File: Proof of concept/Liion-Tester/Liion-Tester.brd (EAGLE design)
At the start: 100 x 80 mm, 22 parts, among them Q1 BC327, Q2 SI4403DDY-T1-GE3, U1 1042, U2 NCP1854FCCT1G, U3 BQ27427YZFR

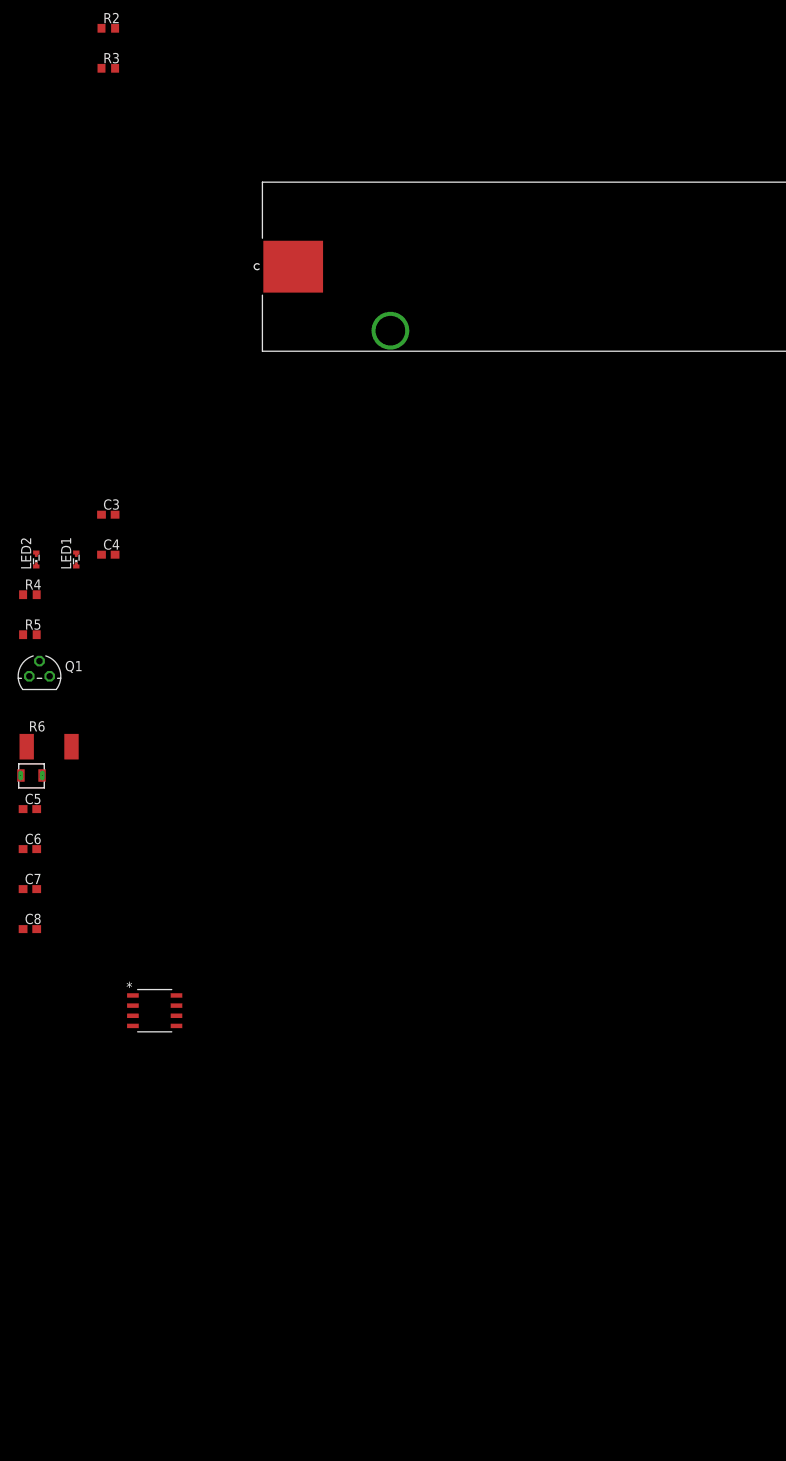
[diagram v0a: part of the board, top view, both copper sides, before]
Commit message: Rework of BQ and NCP. Connector added to schematic.
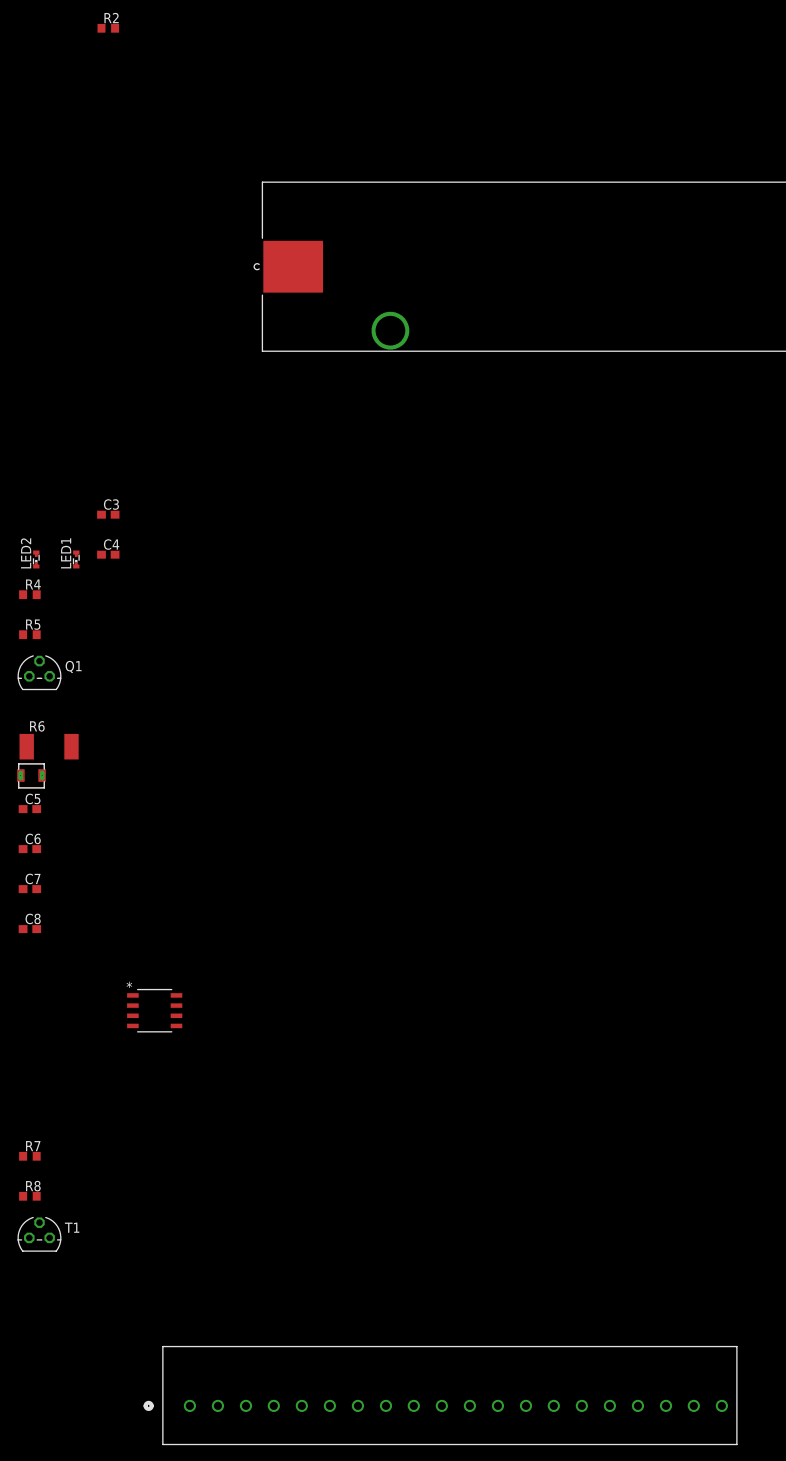
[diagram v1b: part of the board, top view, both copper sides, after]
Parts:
- removed R3: 1M8, rcl:R0603
- added J1: 250-120, custom_library:CONN_250-120_WAG
- added R7, R8: 3k3, rcl:R0603
- added T1: BC337, transistor:TO92
- L1: value 2u2 -> 2.2uH
- renumbered U$1 to L1
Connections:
- removed net GPOUT: R2.1, U3.A1
- removed net VSYS: U3.C2
- new net GPOUT_BQ: J1.5, R2.1, U3.A1
- new net N$9: LED1.A@1, T1.1
- net +5V: now also J1.1, R4.2, R7.2, R8.2; no longer R3.2
- net FTRY: now also J1.9
- net GND: now also J1.2
- net ILIM1: now also J1.10
- net ILIM2: now also J1.11
- net LED_IND: now also J1.6, T1.2; no longer R4.2
- net N$2: no longer R3.1
- net N$4: now also T1.3; no longer LED1.A@1
- net OTG: now also J1.12
- net PACK_P: now also U3.C2
- net SCL: now also J1.3, R7.1
- net SDA: now also J1.4, R8.1
- net SENSN: now also J1.8
- net SPM: now also J1.7
- net TRANS: now also J1.13

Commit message: Final changes in .sch before making .brd
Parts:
- removed J1: 250-120, custom_library:CONN_250-120_WAG
- removed LED1: RED, led:SMARTLED-TTW
- removed Q1: BC327, transistor-pnp:TO92
- removed R4: 3k3, rcl:R0603
- removed T1: BC337, transistor:TO92
- added JUMPERS: (no value), pinhead:2X02
- added MCU: 250-109, custom_library:CONN_250-109_WAG
- added POWER, USB: 250-102, custom_library:CONN_250-102_WAG
- R7, R8: value 3k3 -> 3k3-DNP
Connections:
- removed net N$4: R4.1, T1.3
- removed net N$6: Q1.3, R5.1
- removed net N$9: LED1.A@1, T1.1
- new net BAT_NCP: JUMPERS.3, U2.E5
- new net SRX_BQ: JUMPERS.1, U3.C2
- net +5V: now also POWER.1; no longer J1.1, R4.2, R5.2
- net FTRY: now also MCU.7; no longer J1.9
- net GND: now also POWER.2; no longer J1.2, LED1.C@1
- net GPOUT_BQ: now also MCU.3; no longer J1.5
- net ILIM1: now also MCU.8; no longer J1.10
- net ILIM2: now also MCU.9; no longer J1.11
- net LED_IND: now also MCU.4, R5.2; no longer J1.6, Q1.2, T1.2
- net N$5: now also R5.1; no longer Q1.1
- net OTG: now also USB.1; no longer J1.12
- net PACK_P: now also JUMPERS.2, JUMPERS.4; no longer U2.E5, U3.C2
- net SCL: now also MCU.1; no longer J1.3
- net SDA: now also MCU.2; no longer J1.4
- net SENSN: now also MCU.6; no longer J1.8
- net SPM: now also MCU.5; no longer J1.7
- net TRANS: now also USB.2; no longer J1.13

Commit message: Version control
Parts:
- R7, R8: value 3k3-DNP -> DNP-3k3
- moved JUMPERS 370.6 mm to (34.4, 51.4), turned to 180 degrees
- moved MCU 353.4 mm to (62.6, 49.8)
- moved USB 311.3 mm to (53.4, 49.8)
- moved POWER 296.6 mm to (44.2, 49.8)
- moved R8 277.6 mm to (66.0, 54.0), flipped to the bottom, turned to 90 degrees
- moved R7 271.8 mm to (62.6, 54.0), flipped to the bottom, turned to 90 degrees
- moved C8 262.3 mm to (62.0, 72.6), flipped to the bottom, turned to 180 degrees
- moved Q2 262.2 mm to (70.2, 64.6), flipped to the bottom, turned to 180 degrees
- moved C7 256.0 mm to (57.2, 72.6), flipped to the bottom, turned to 180 degrees
- moved C6 251.6 mm to (66.8, 69.6), flipped to the bottom, turned to 180 degrees
- moved C5 245.3 mm to (53.2, 72.6), flipped to the bottom, turned to 180 degrees
- moved L1 237.7 mm to (54.0, 68.6), flipped to the bottom, turned to 270 degrees
- moved R6 236.3 mm to (60.6, 69.2), flipped to the bottom
- moved R5 217.2 mm to (60.4, 62.0), flipped to the bottom, turned to 90 degrees
- moved C4 205.5 mm to (53.8, 65.6), flipped to the bottom
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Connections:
- net BAT_NCP: now also JUMPERS.1; no longer JUMPERS.3
- net SRX_BQ: now also JUMPERS.3; no longer JUMPERS.1
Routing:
- net PACK_P: track 0.00 -> 103.2 mm, vias 0 -> 3
- net +5V: track 0.00 -> 58.2 mm, vias 0 -> 2
- net SDA: track 0.00 -> 43.5 mm, vias 0 -> 3
- net SENSN: track 0.00 -> 40.2 mm, vias 0 -> 1
- net SCL: track 0.00 -> 37.5 mm, vias 0 -> 2
- net BAT_NCP: track 0.00 -> 34.9 mm, vias 0 -> 1
- net SPM: track 0.00 -> 34.4 mm
- net FTRY: track 0.00 -> 31.5 mm
- net N$5: track 0.00 -> 27.4 mm, vias 0 -> 3
- net SRX_BQ: track 0.00 -> 21.8 mm, vias 0 -> 1
- net LED_IND: track 0.00 -> 21.7 mm
- net N$7: track 0.00 -> 11.8 mm
- net FET: track 0.00 -> 9.98 mm
- net CBOOT: track 0.00 -> 9.08 mm, vias 0 -> 2
- net TRANS: track 0.00 -> 8.96 mm, vias 0 -> 1
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- added copper zone on layer 1, net GND
- added copper zone on layer 16, net GND

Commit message: Finished .brd with changes in schematic
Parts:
- removed LED2: GREEN, led:SMARTLED-TTW
- added LED1: FYLS-1206PGC, custom_library:LED_QBLP650_1206_QTB
- moved R7 10.0 mm to (69.6, 46.8), turned to 270 degrees
- moved R8 7.20 mm to (66.2, 46.8), turned to 270 degrees
- moved L1 5.43 mm to (48.6, 69.2), turned to 90 degrees
- moved C8 5.00 mm to (57.0, 72.6)
- moved C7 3.60 mm to (60.8, 72.6)
- moved R6 2.81 mm to (57.8, 69.0)
- moved JUMPERS 1.22 mm to (33.2, 51.2)
- moved U2 0.85 mm to (58.0, 65.2)
- moved R1 0.45 mm to (37.0, 68.0)
- moved U3 0.28 mm to (40.7, 68.1)
- moved C4 0.28 mm to (53.6, 65.8)
- moved C3 0.20 mm to (53.6, 63.4)
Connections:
- removed net N$5: LED2.A@1, R5.1
- new net N$4: LED1.2, R5.1
- net FTRY: now also MCU.6; no longer MCU.7
- net GND: now also LED1.1; no longer LED2.C@1
- net GPOUT_BQ: now also MCU.5; no longer MCU.3
- net ILIM2: now also MCU.7; no longer MCU.9
- net OTG: now also USB.2; no longer USB.1
- net SCL: now also MCU.3; no longer MCU.1
- net SENSN: now also MCU.9; no longer MCU.6
- net SPM: now also MCU.1; no longer MCU.5
- net TRANS: now also USB.1; no longer USB.2
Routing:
- net GPOUT_BQ: track 2.68 -> 57.4 mm, vias 0 -> 3
- net ILIM1: track 0.00 -> 35.1 mm
- net ILIM2: track 0.00 -> 31.6 mm
- net N$5: track 27.4 -> 0.00 mm, vias 3 -> 0
- net N$4: track 0.00 -> 24.8 mm, vias 0 -> 1
- net OTG: track 0.00 -> 16.6 mm, vias 0 -> 3
- net TRANS: track 8.96 -> 25.1 mm, vias 1 -> 3
- net SPM: track 34.4 -> 18.4 mm, vias 0 -> 2
- net SENSN: track 40.2 -> 55.6 mm, vias 1 -> 0
- net SENSP: track 4.11 -> 12.0 mm, vias 0 -> 2
- net N$8: track 0.00 -> 7.41 mm
- net SCL: track 37.5 -> 42.7 mm, vias 2 -> 3
- net BAT_NCP: track 34.9 -> 39.2 mm, vias 1 -> 4
- net +5V: track 58.2 -> 62.3 mm, vias 2 -> 1
- net N$7: track 11.8 -> 15.5 mm, vias 0 -> 2
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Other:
- board size 100 x 80 mm -> 89 x 42 mm
- board text added: "+5V"
- board text added: "BAT_NCP"
- board text added: "FTRY"
- board text added: "GND"
- board text added: "GP-BQ"
- board text added: "ILIM1"
- board text added: "ILIM2"
- board text added: "LED"
- board text added: "LI-ION +"
- board text added: "LI-ION GND"
- board text added: "OTG"
- board text added: "PACK_P"
- board text added: "SCL"
- board text added: "SDA"
- board text added: "SENSN"
- board text added: "SPM"
- board text added: "SRX_BQ"
- board text added: "TRANS"

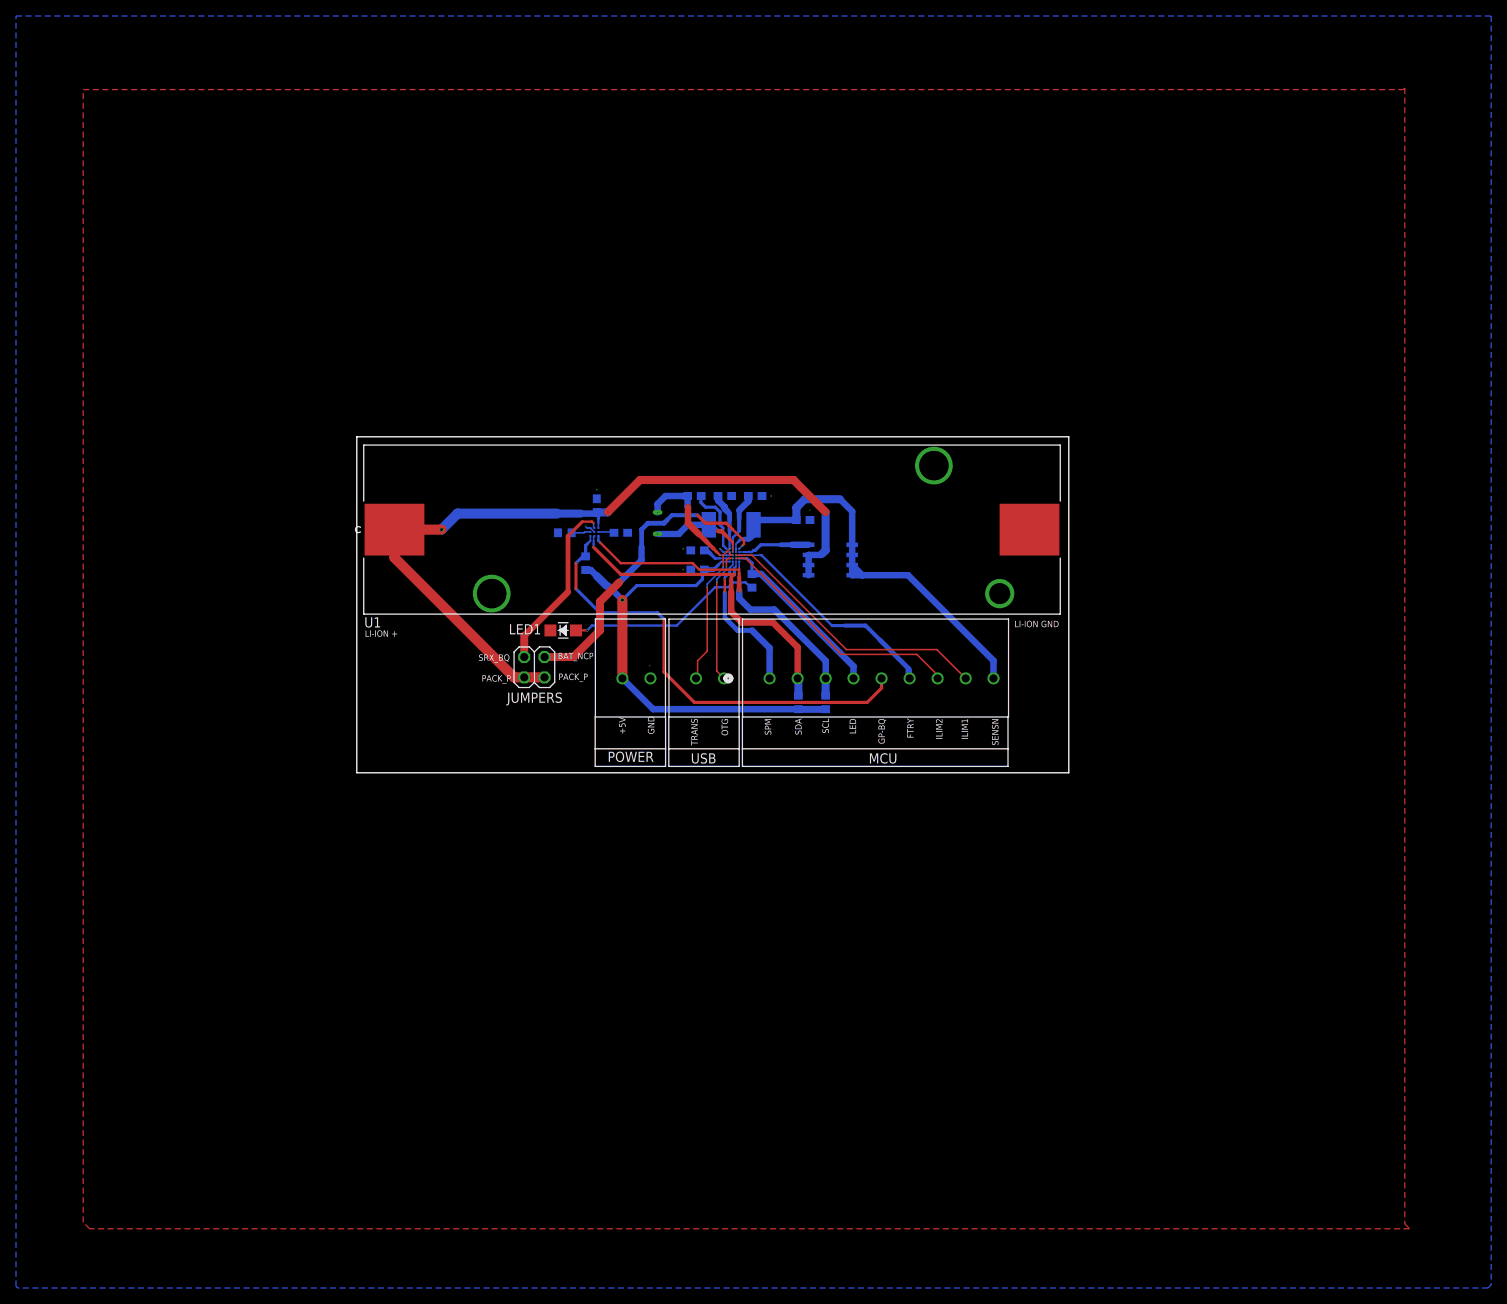
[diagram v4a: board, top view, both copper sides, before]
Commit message: Added polygons for PACK_P and SENS_N
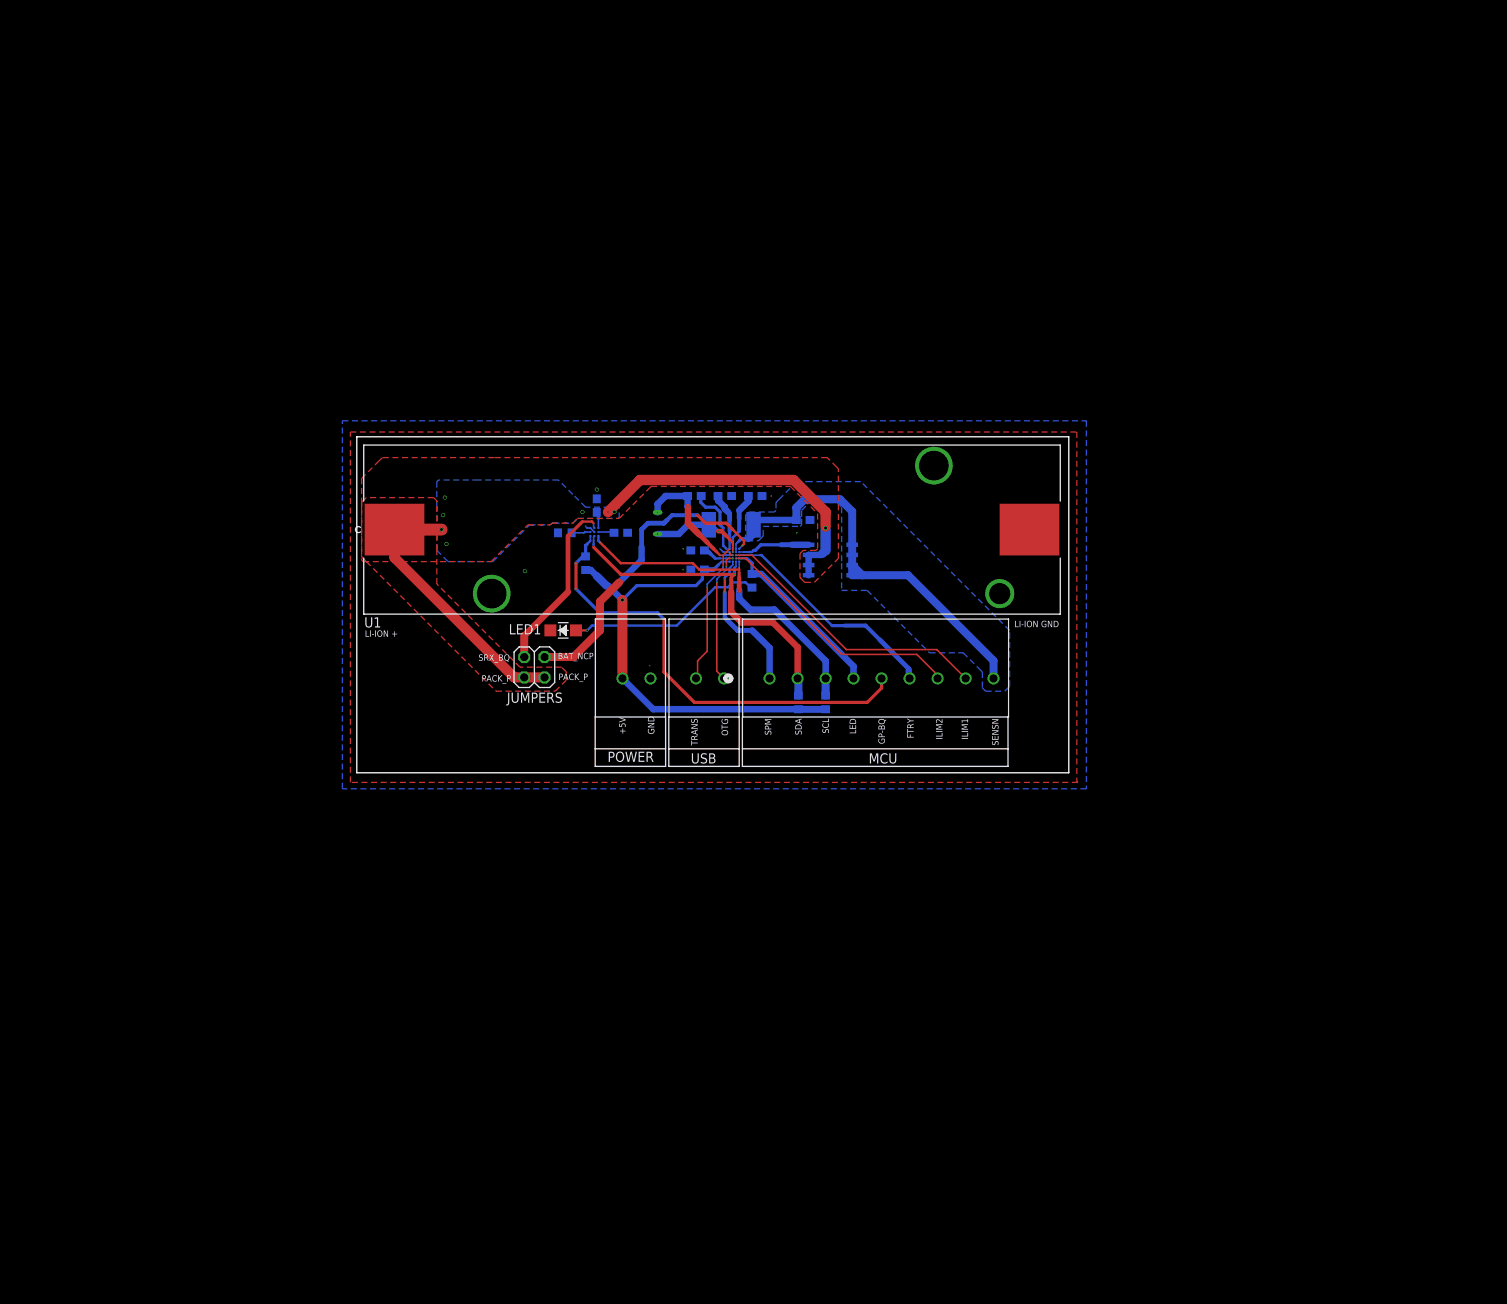
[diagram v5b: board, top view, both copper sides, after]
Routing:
- net PACK_P: track 99.5 -> 77.5 mm, vias 3 -> 8
- net GND: vias 10 -> 11
- added copper zone on layer 1, net PACK_P
- added copper zone on layer 16, net PACK_P
- added copper zone on layer 16, net SENSN
